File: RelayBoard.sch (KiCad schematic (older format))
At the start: 129 parts, among them P1 HE10-32, Q1 NPN, Q10 NPN, Q11 NPN, Q12 NPN, Q13 NPN, Q14 NPN, Q15 NPN, Q16 NPN, Q17 NPN, Q18 NPN, Q19 NPN, Q2 NPN, Q20 NPN, Q21 NPN, Q22 NPN, Q23 NPN, Q24 NPN, Q25 NPN, Q26 NPN, Q27 NPN, Q28 NPN, Q29 NPN, Q3 NPN, Q30 NPN, Q31 NPN, Q32 NPN, Q4 NPN, Q5 NPN, Q6 NPN, Q7 NPN, Q8 NPN, Q9 NPN

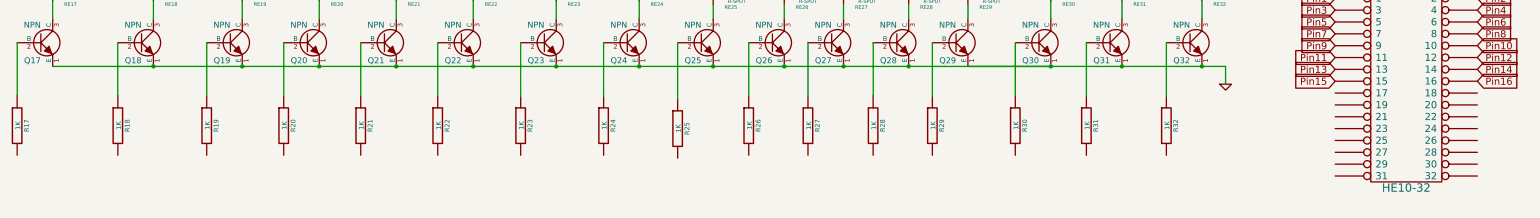
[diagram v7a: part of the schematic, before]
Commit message: Finished Pins 17 to 24, they are now connected to the bus
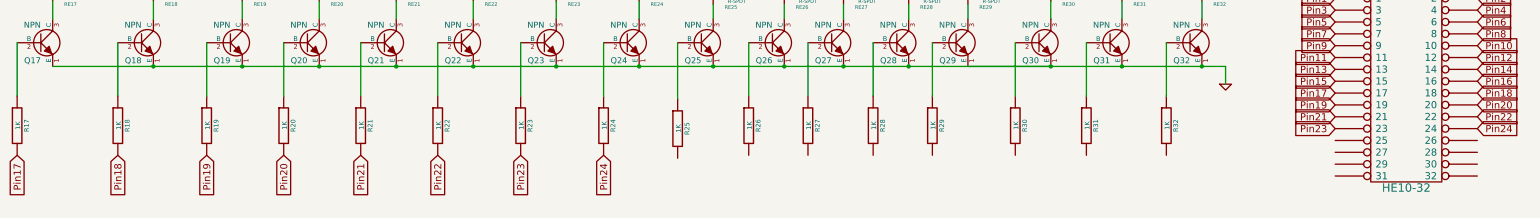
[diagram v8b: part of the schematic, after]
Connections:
- net Pin17: now reaches P1.17
- net Pin17: now also R17.2
- net Pin18: now reaches P1.18
- net Pin18: now also R18.2
- net Pin19: now reaches P1.19
- net Pin19: now also R19.2
- net Pin20: now reaches P1.20
- net Pin20: now also R20.2
- net Pin21: now reaches P1.21
- net Pin21: now also R21.2
- net Pin22: now reaches P1.22
- net Pin22: now also R22.2
- net Pin23: now reaches P1.23
- net Pin23: now also R23.2
- net Pin24: now reaches P1.24
- net Pin24: now also R24.2
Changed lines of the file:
@@
 Text GLabel 12925 5550 2    60   Input ~ 0
 Pin16
+Text GLabel 600  6175 3    60   Input ~ 0
+Pin17
+Text GLabel 1450 6175 3    60   Input ~ 0
+Pin18
+Text GLabel 2200 6175 3    60   Input ~ 0
+Pin19
+Text GLabel 2850 6175 3    60   Input ~ 0
+Pin20
+Text GLabel 3500 6175 3    60   Input ~ 0
+Pin21
+Text GLabel 4150 6175 3    60   Input ~ 0
+Pin22
+Text GLabel 4850 6175 3    60   Input ~ 0
+Pin23
+Text GLabel 5550 6175 3    60   Input ~ 0
+Pin24
+Text GLabel 11725 5650 0    60   Input ~ 0
+Pin17
+Text GLabel 12925 5650 2    60   Input ~ 0
+Pin18
+Text GLabel 11725 5750 0    60   Input ~ 0
+Pin19
+Text GLabel 12925 5750 2    60   Input ~ 0
+Pin20
+Text GLabel 11725 5850 0    60   Input ~ 0
+Pin21
+Text GLabel 12925 5850 2    60   Input ~ 0
+Pin22
+Text GLabel 11725 5950 0    60   Input ~ 0
+Pin23
+Text GLabel 12925 5950 2    60   Input ~ 0
+Pin24
 $EndSCHEMATC
